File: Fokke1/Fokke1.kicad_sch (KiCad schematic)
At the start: 28 parts, among them J101 Conn_01x20_Male, SW101 SW_SPST, SW102 SW_SPST, SW103 SW_SPST, SW104 SW_SPST, SW105 SW_SPST, SW106 SW_SPST, SW107 SW_SPST, SW108 SW_SPST, SW109 SW_SPST

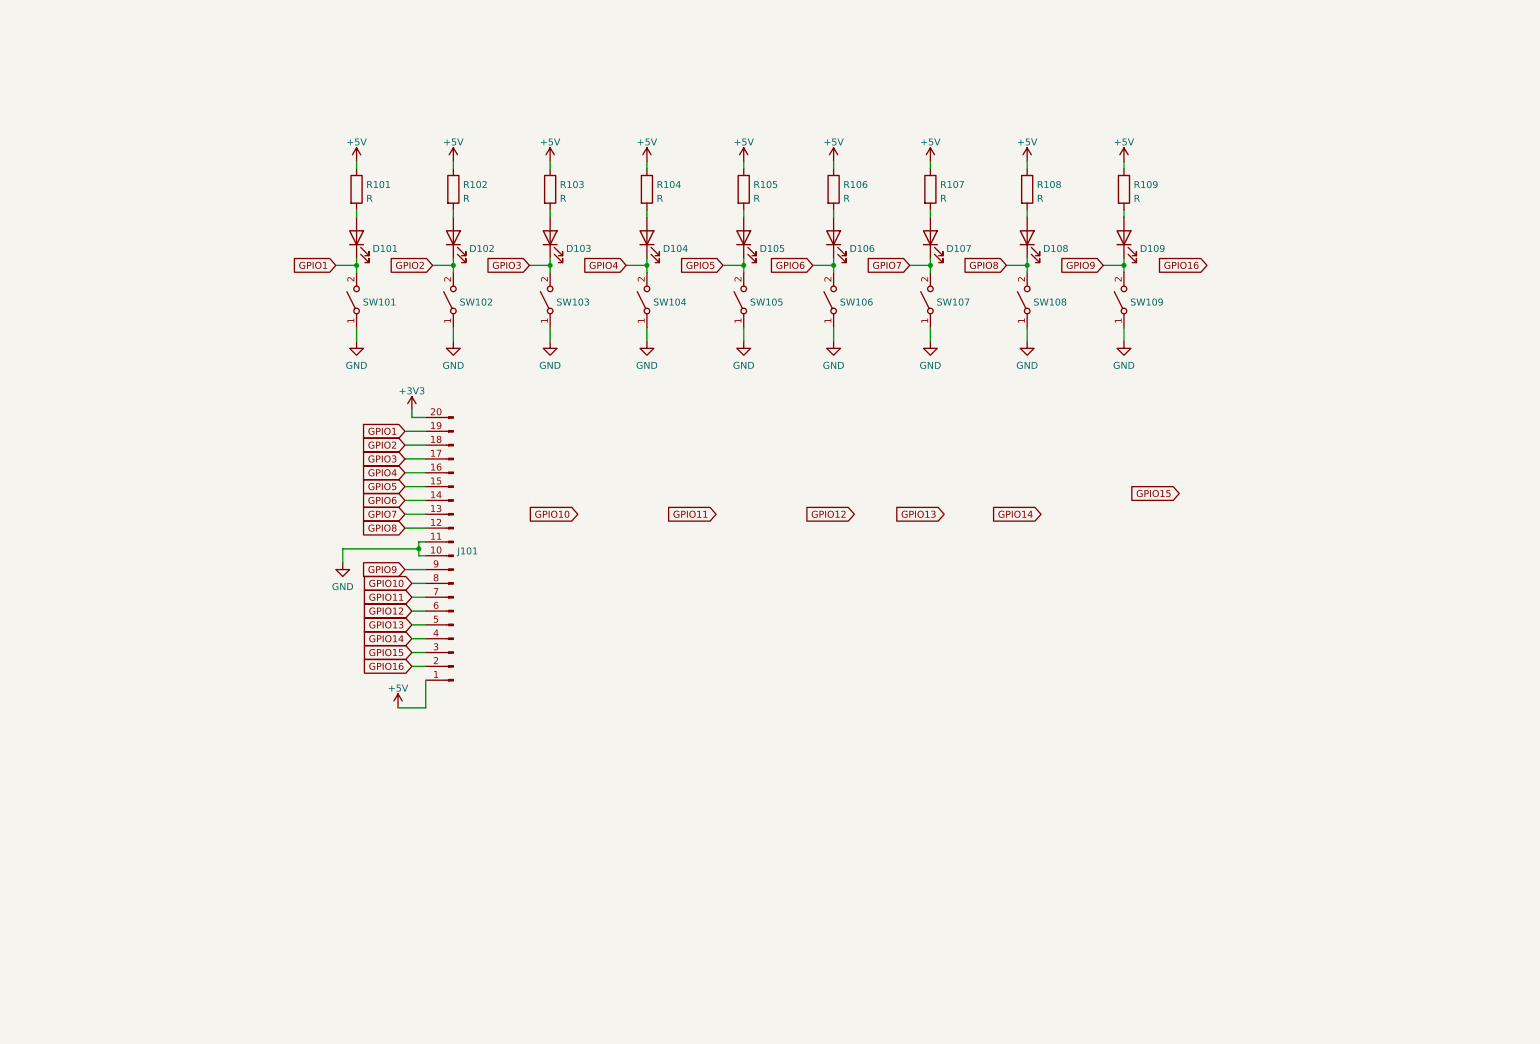
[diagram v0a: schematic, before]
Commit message: added logo and layout plans
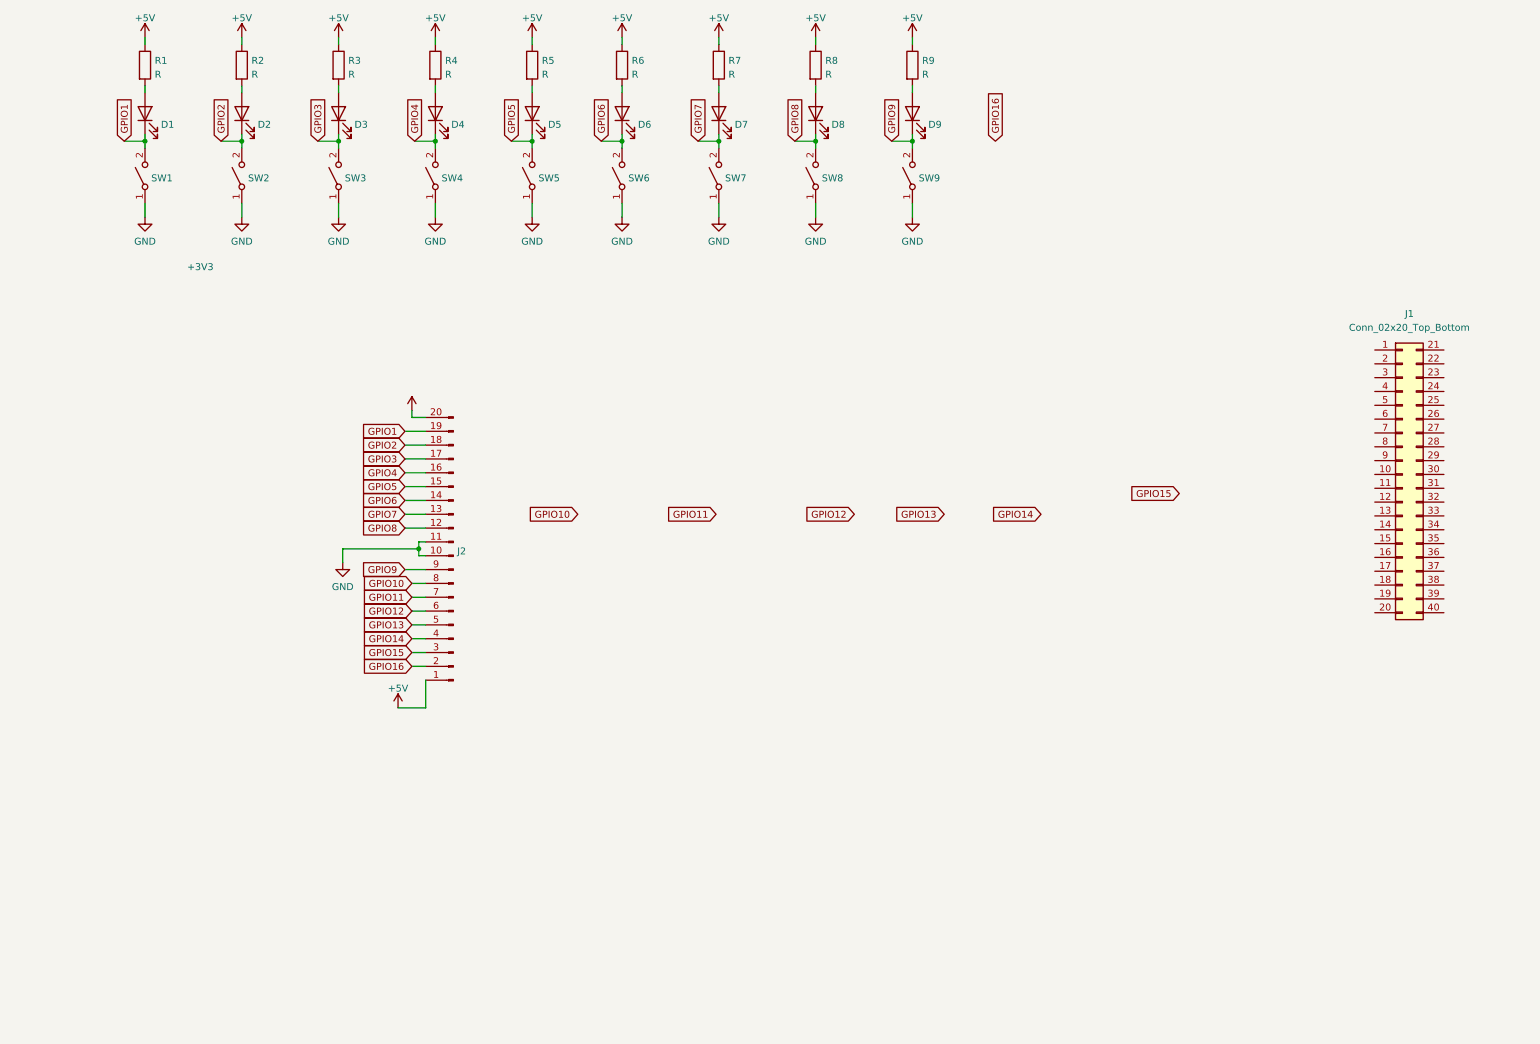
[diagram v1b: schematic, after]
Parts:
- added J1: Conn_02x20_Top_Bottom, symbol Connector_Generic:Conn_02x20_Top_Bottom
- renumbered D101 to D1, D102 to D2, D103 to D3, D104 to D4, D105 to D5, D106 to D6, D107 to D7, D108 to D8, D109 to D9, J101 to J2, R101 to R1, R102 to R2, R103 to R3, R104 to R4, R105 to R5, R106 to R6, R107 to R7, R108 to R8, R109 to R9, SW101 to SW1, SW102 to SW2, SW103 to SW3, SW104 to SW4, SW105 to SW5, SW106 to SW6, SW107 to SW7, SW108 to SW8, SW109 to SW9
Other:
- moved on the sheet: D1, D2, D3, D4, D5, D6, D7, D8, D9, R1, R2, R3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

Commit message: I am halfway of schematic of Fokke1. I need to make me new footprints for leds and resistors and switches because I want to remove and add certain silk texts
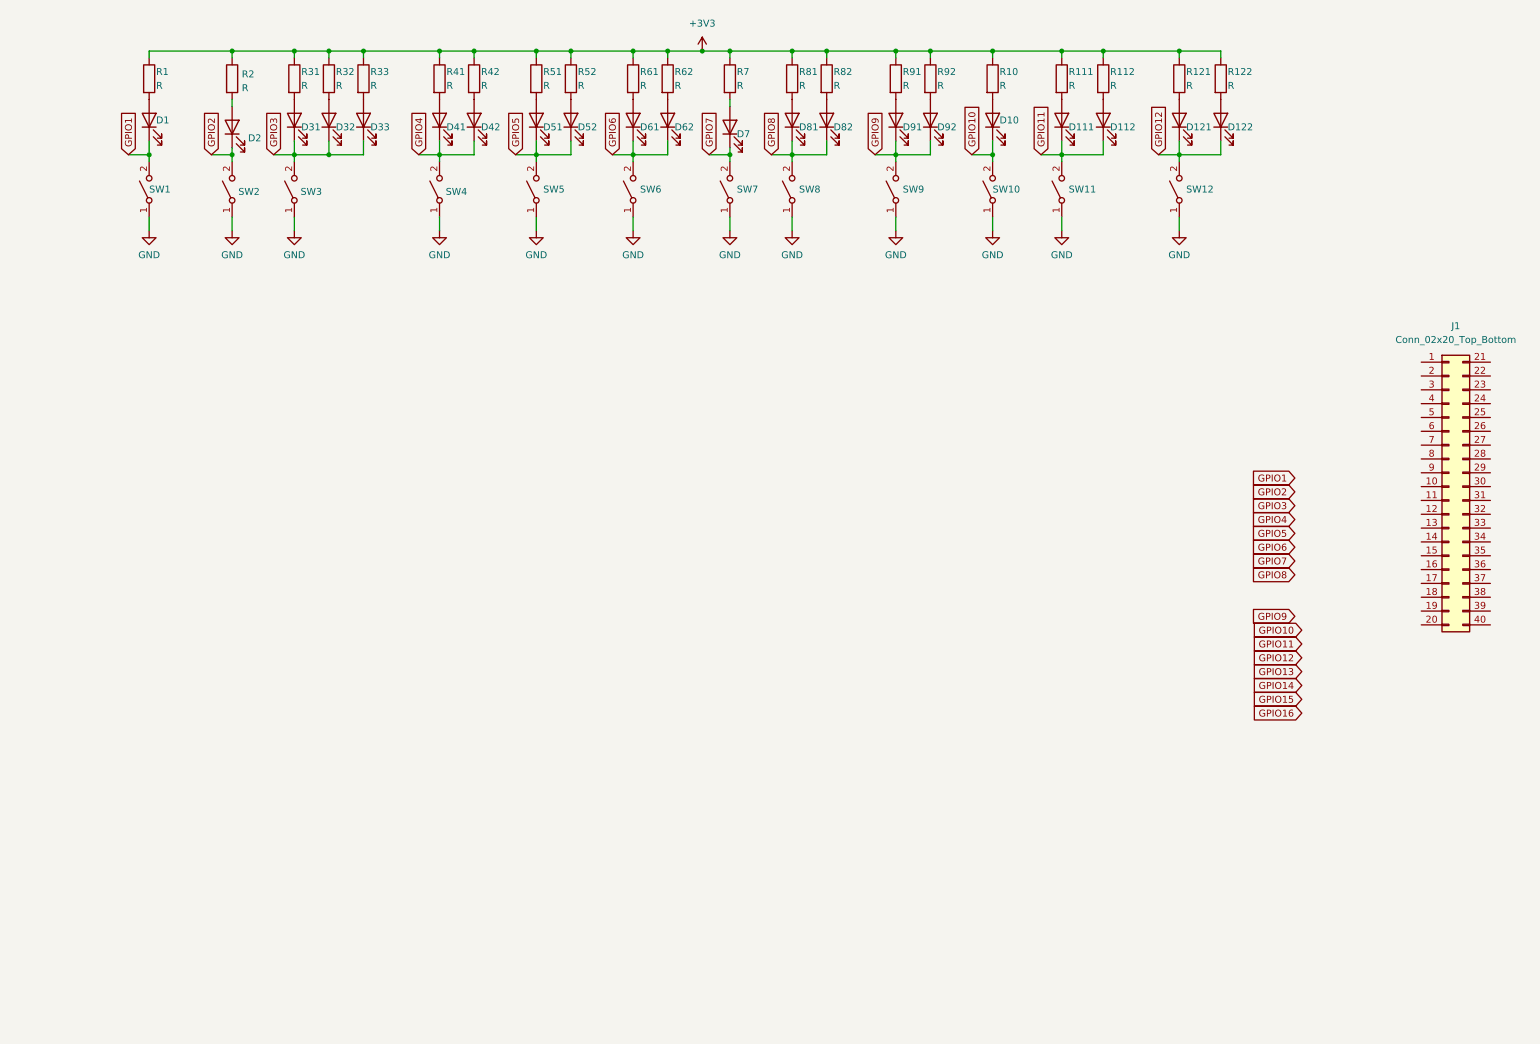
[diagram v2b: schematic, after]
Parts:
- removed D5, D6, D8, D9: LED, LED_THT:LED_D3.0mm, symbol Device:LED
- removed J2: Conn_01x20_Male, Connector_PinHeader_2.54mm:PinHeader_1x20_P2.54mm_Vertical, symbol Connector:Conn_01x20_Male
- removed R5, R6, R8, R9: R, Resistor_SMD:R_0805_2012Metric_Pad1.20x1.40mm_HandSolder, symbol Device:R
- added D10, D111, D112, D121, D122, D32, D33, D42, D51, D52, D61, D62, D81, D82, D91, D92: LED, LED_THT:LED_D3.0mm, symbol Device:LED
- added R10, R111, R112, R121, R122, R32, R33, R42, R51, R52, R61, R62, R81, R82, R91, R92: R, Resistor_SMD:R_0805_2012Metric_Pad1.20x1.40mm_HandSolder, symbol Device:R
- added SW10, SW11, SW12: SW_SPST, Button_Switch_THT:SW_PUSH_6mm_H4.3mm, symbol Switch:SW_SPST
- renumbered D3 to D31, D4 to D41, R3 to R31, R4 to R41
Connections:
- net +5V is gone; now on net +3V3: R1.1, R2.1, R31.1, R41.1, R7.1
- net +3V3: now also R10.1, R111.1, R112.1, R121.1, R122.1, R32.1, R33.1, R42.1, R51.1, R52.1, R61.1, R62.1, R81.1, R82.1, R91.1, R92.1
- net GND: now also SW10.1 (A), SW11.1 (A), SW12.1 (A)
- net GPIO10: now also D10.1 (K), SW10.2 (B)
- net GPIO11: now also D111.1 (K), D112.1 (K), SW11.2 (B)
- net GPIO12: now also D121.1 (K), D122.1 (K), SW12.2 (B)
- net GPIO3: now also D32.1 (K), D33.1 (K)
- net GPIO4: now also D42.1 (K)
- net GPIO5: now also D51.1 (K), D52.1 (K)
- net GPIO6: now also D61.1 (K), D62.1 (K)
- net GPIO8: now also D81.1 (K), D82.1 (K)
- net GPIO9: now also D91.1 (K), D92.1 (K)
- new net: D32.2 (A), R32.2
- new net: D111.2 (A), R111.2
- new net: D10.2 (A), R10.2
- new net: D52.2 (A), R52.2
- new net: D82.2 (A), R82.2
- new net: D112.2 (A), R112.2
- new net: D122.2 (A), R122.2
- new net: D51.2 (A), R51.2
- new net: D33.2 (A), R33.2
- new net: D42.2 (A), R42.2
- new net: D121.2 (A), R121.2
- new net: D91.2 (A), R91.2
- new net: D81.2 (A), R81.2
- new net: D62.2 (A), R62.2
- new net: D61.2 (A), R61.2
- new net: D92.2 (A), R92.2
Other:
- moved on the sheet: D1, D2, D31, D41, J1, R1, R2, R31, R41, SW1, SW2, SW3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

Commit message: Did all component numbering for Fokke1. The connector is still to be finished
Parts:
- added D1314, D132, D142, D151, D152, D161, D162, D171, D172, D1819, D182, D192, D201, D202, D211, D212, D221, D222: LED, custom_kicad_lib_sk:LED_NO_SILK, symbol Device:LED
- added D3, D4, D5, D6: D, Diode_SMD:D_SOD-123, symbol Device:D
- added R132, R142, R152, R162, R172, R182, R192, R202, R212, R222: 3k3, custom_kicad_lib_sk:R_0805_SILK_VALUE, symbol Device:R
- added R151, R161, R171, R201, R211, R221: 1k5, custom_kicad_lib_sk:R_0805_SILK_VALUE, symbol Device:R
- added R1819, R3: 1k, custom_kicad_lib_sk:R_0805_SILK_VALUE, symbol Device:R
- D1, D10, D111, D112, D121, D122, D2, D31, D32, D33, D41, D42, D51, D52, D61, D62, D7, D81, D82, D91, D92: footprint LED_THT:LED_D3.0mm -> custom_kicad_lib_sk:LED_NO_SILK
- J1: footprint (none) -> Connector_PinHeader_2.54mm:PinHeader_2x20_P2.54mm_Vertical_SMD
- R1, R10, R111, R112, R121, R122, R2, R31, R32, R33, R41, R42, R51, R52, R61, R62, R7, R81, R82, R91, R92: value R -> 1k5; footprint Resistor_SMD:R_0805_2012Metric_Pad1.20x1.40mm_HandSolder -> custom_kicad_lib_sk:R_0805_SILK_VALUE
- SW1, SW10, SW11, SW12, SW2, SW3, SW4, SW5, SW6, SW7, SW8, SW9: footprint Button_Switch_THT:SW_PUSH_6mm_H4.3mm -> custom_kicad_lib_sk:SW_NO_SILK
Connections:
- net +3V3: now also R151.1, R161.1, R171.1, R1819.1, R201.1, R211.1, R221.1, R3.1
- net GND: now also D132.1 (K), D142.1 (K), D152.1 (K), D162.1 (K), D172.1 (K), D182.1 (K), D192.1 (K), D202.1 (K), D212.1 (K), D222.1 (K)
- net GPIO13: now also D3.1 (K), R132.1
- net GPIO14: now also D4.1 (K), R142.1
- net GPIO15: now also D151.1 (K), R152.1
- net GPIO16: now also D161.1 (K), R162.1
- new net: D1314.2 (A), R3.2
- new net: D202.2 (A), R202.2
- new net: D212.2 (A), R212.2
- new net: D192.2 (A), R192.2
- new net: D152.2 (A), R152.2
- new net: D1314.1 (K), D3.2 (A), D4.2 (A)
- new net: D142.2 (A), R142.2
- new net: D201.2 (A), R201.2
- new net: D171.2 (A), R171.2
- new net: D162.2 (A), R162.2
- new net: D221.2 (A), R221.2
- new net: D222.2 (A), R222.2
- new net: D172.2 (A), R172.2
- new net: D161.2 (A), R161.2
- new net: D211.2 (A), R211.2
- new net: D151.2 (A), R151.2
- new net: D1819.1 (K), D5.2 (A), D6.2 (A)
- new net: D1819.2 (A), R1819.2
- new net: D182.2 (A), R182.2
- new net: D132.2 (A), R132.2
- new net GPIO17: D171.1 (K), R172.1
- new net GPIO18: D5.1 (K), R182.1
- new net GPIO19: D6.1 (K), R192.1
- new net GPIO20: D201.1 (K), R202.1
- new net GPIO21: D211.1 (K), R212.1
- new net GPIO22: D221.1 (K), R222.1
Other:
- note added: "1"
- note added: "1 bend"
- note added: "10"
- note added: "2"
- note added: "2 straight"
- note added: "3"
- note added: "4"
- note added: "5"
- note added: "6"
- note added: "7"
- note added: "8"
- note added: "9"

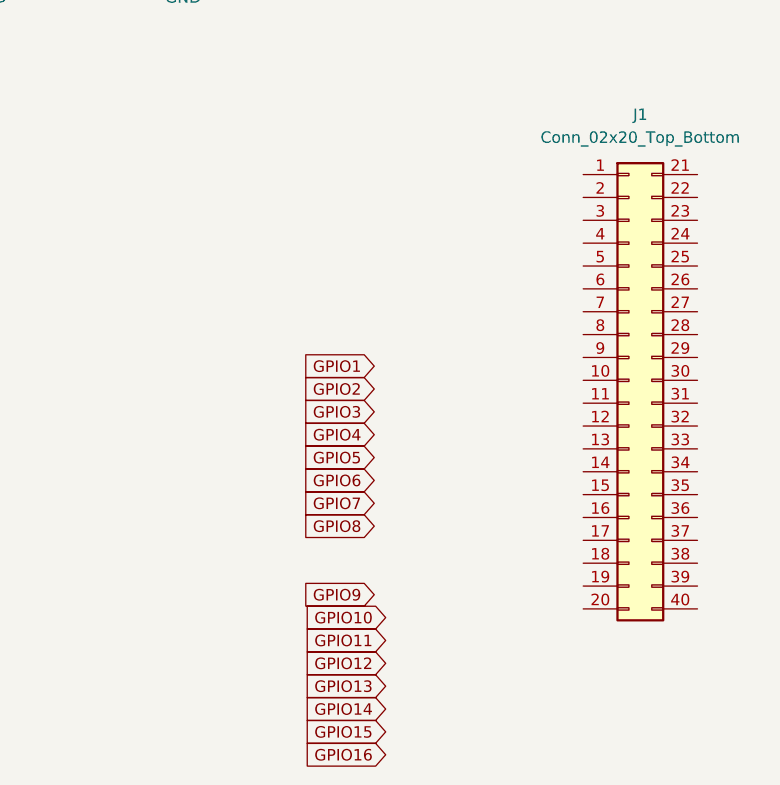
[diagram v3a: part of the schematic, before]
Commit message: routed all but the main connector of Fokke1
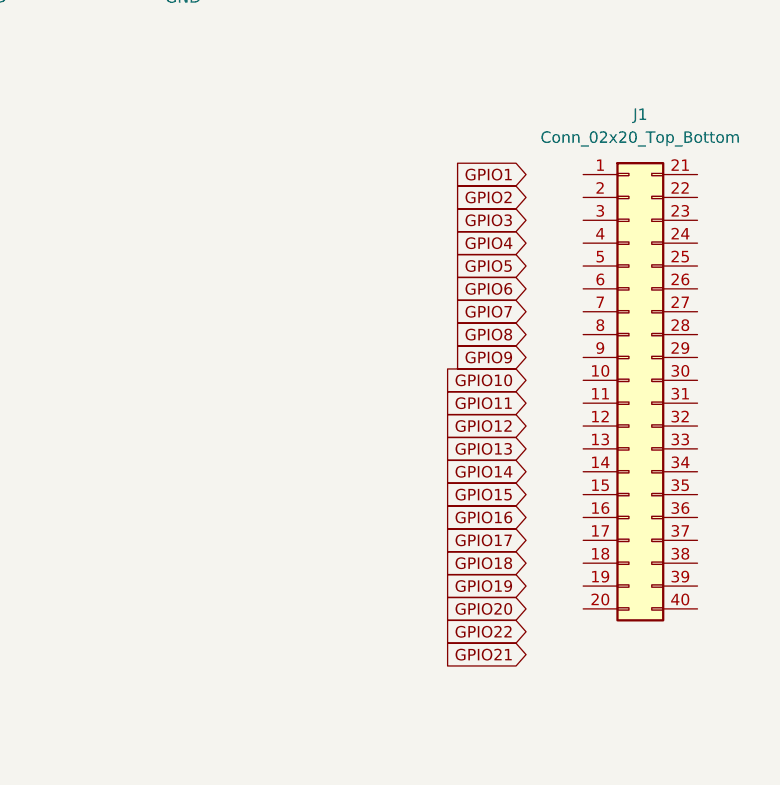
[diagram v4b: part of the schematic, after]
